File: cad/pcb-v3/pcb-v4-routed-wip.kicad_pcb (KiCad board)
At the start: 4 copper layers, 19.3 x 19.3 mm, 50 parts

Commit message: KiCad rewrites track geometry on format migration -- keep-out needs slack
The fill cleared blocker 18 and blocker 7 came back: three GND segments inside
the antenna keep-out, at coordinates that did not exist in the file I saved.

Diagnosis: not KiCad's fill and not the pour. Segment COUNT was identical in
and out (554), the keep-out polygons were byte-identical, but the geometry
moved. Opening the board migrated it from file format 20240108 to 20260206,
and the migration rewrote track geometry -- a tap path that skirted the
keep-out came back as a diagonal cutting the corner. Deepest copper intrusion
0.2635 mm.

So the previous commit's fix was necessary but not sufficient: honouring
'tracks not_allowed' stops US routing into the zone, and does nothing about
KiCad re-routing afterwards. The mask is now GROWN by halo + KEEPOUT_MARGIN
(0.30) to leave slack for whatever it simplifies into.

Two corrections to myself in this one:
  * my 'tracks not_allowed' fix carried a comment saying the mask was grown by
    the halo. It was not -- the comment described an intention, the code did
    a bare OR. Now there is a real _grow().
  * I first reached for 0.15 mm of margin and wrote that it 'covers it 10x
    over'. It does not: 0.15 < 0.2635, so it would have left the deepest
    intrusion in place. Sized from the measurement instead.

Costs 4 taps (24 -> 20). Paid deliberately -- copper in the antenna zone
cannot be seen, cannot be checked against a drawing, and ships as 'the radio
is mysteriously worse than it should be'.
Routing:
- net GND: track 11.8 -> 10.5 mm, vias 24 -> 20
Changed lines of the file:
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@@
 		)
 	)
-	(segment (start 5.7500 5.1500) (end 5.6500 5.1500) (width 0.127) (layer "F.Cu") (net 4))
-	(segment (start 5.6500 5.1500) (end 5.4000 4.9000) (width 0.127) (layer "F.Cu") (net 4))
-	(segment (start 5.4000 4.9000) (end 4.8000 4.9000) (width 0.127) (layer "F.Cu") (net 4))
-	(segment (start 4.8000 4.9000) (end 4.5000 4.6000) (width 0.127) (layer "F.Cu") (net 4))
 	(segment (start 2.8500 -8.6000) (end 2.6000 -8.8000) (width 0.127) (layer "F.Cu") (net 4))
 	(segment (start 2.6000 -8.8000) (end 1.5500 -8.8000) (width 0.127) (layer "F.Cu") (net 4))
 	(segment (start -3.4500 -8.6000) (end -3.6500 -8.6000) (width 0.127) (layer "F.Cu") (net 4))
 	(segment (start -3.6500 -8.6000) (end -3.7500 -8.5000) (width 0.127) (layer "F.Cu") (net 4))
-	(segment (start 6.1500 -8.3500) (end 6.4000 -8.6000) (width 0.127) (layer "F.Cu") (net 4))
+	(segment (start 5.6500 -8.3500) (end 6.0000 -8.7000) (width 0.127) (layer "F.Cu") (net 4))
 	(segment (start -8.3000 -3.3000) (end -8.6000 -3.3000) (width 0.127) (layer "B.Cu") (net 4))
 	(segment (start -8.6000 -3.3000) (end -8.9000 -3.6000) (width 0.127) (layer "B.Cu") (net 4))
@@
 	(segment (start -7.9000 1.7000) (end -8.2000 1.9500) (width 0.127) (layer "F.Cu") (net 4))
 	(segment (start -4.9500 -8.5500) (end -4.1000 -8.5500) (width 0.127) (layer "F.Cu") (net 4))
-	(via (at 4.5000 4.6000) (size 0.45) (drill 0.2) (layers "F.Cu" "B.Cu") (net 4))
-	(via (at 5.7500 6.9000) (size 0.45) (drill 0.2) (layers "F.Cu" "B.Cu") (net 4))
 	(via (at -3.9000 -8.4500) (size 0.45) (drill 0.2) (layers "F.Cu" "B.Cu") (net 4))
 	(via (at 7.1000 7.1500) (size 0.45) (drill 0.2) (layers "F.Cu" "B.Cu") (net 4))
 	(via (at -1.6500 -8.6000) (size 0.45) (drill 0.2) (layers "F.Cu" "B.Cu") (net 4))
 	(via (at 1.5500 -8.8000) (size 0.45) (drill 0.2) (layers "F.Cu" "B.Cu") (net 4))
-	(via (at 6.4000 -8.6000) (size 0.45) (drill 0.2) (layers "F.Cu" "B.Cu") (net 4))
+	(via (at 6.0000 -8.7000) (size 0.45) (drill 0.2) (layers "F.Cu" "B.Cu") (net 4))
 	(via (at -7.0000 2.7000) (size 0.45) (drill 0.2) (layers "F.Cu" "B.Cu") (net 4))
 	(via (at 1.0500 -8.3500) (size 0.45) (drill 0.2) (layers "F.Cu" "B.Cu") (net 4))
@@
 	(via (at 7.7500 7.1500) (size 0.45) (drill 0.2) (layers "F.Cu" "B.Cu") (net 4))
 	(via (at 4.7000 -6.4000) (size 0.45) (drill 0.2) (layers "F.Cu" "B.Cu") (net 4))
-	(via (at -5.7500 4.5500) (size 0.45) (drill 0.2) (layers "F.Cu" "B.Cu") (net 4))
 	(via (at -5.5500 -6.0000) (size 0.45) (drill 0.2) (layers "F.Cu" "B.Cu") (net 4))
 	(via (at -5.1500 3.4500) (size 0.45) (drill 0.2) (layers "F.Cu" "B.Cu") (net 4))
-	(via (at 3.5500 4.5500) (size 0.45) (drill 0.2) (layers "F.Cu" "B.Cu") (net 4))
 	(via (at 5.8500 -2.2500) (size 0.45) (drill 0.2) (layers "F.Cu" "B.Cu") (net 4))
 	(via (at 7.3000 -2.1000) (size 0.45) (drill 0.2) (layers "F.Cu" "B.Cu") (net 4))

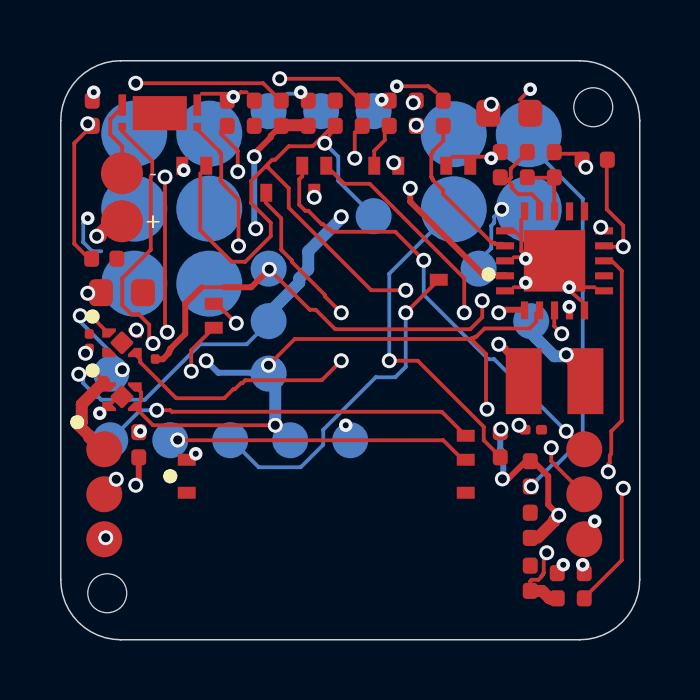
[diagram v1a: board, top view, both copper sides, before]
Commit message: gnd_taps: prune stub segments with a free end (and the custom-pad trap, again)
preflight check 20 caught two GND stubs on the filled board: (-8.30,-3.30),
which touched nothing at EITHER end, and (-2.10,-8.55), which ran from a via
to nowhere. Neither carried current, but a stub is an antenna, a yield
question, and a lie in the file about what is connected.

gnd_taps now prunes any tap segment whose end does not land on a GND pad, one
of its own vias, pre-existing GND copper, or another tap. Iterative, because
dropping a stub can orphan whatever fed it.

THE FIRST VERSION OF THIS PRUNE WAS WRONG and pruned 10 of 23 segments. Its
anchor test used max(w,h)/2, which for U3/U4 is the 0.1485 mm ANCHOR of a
custom pad, not its copper -- so every segment correctly landing on one looked
unanchored. That is the THIRD time this exact trap has bitten on this board
(stitch_open's masks, gnd_taps' own clearance masks, now this), and
pad_radius() -- the function written to avoid it -- was already defined 200
lines above. Fixed to use it: 4 stubs pruned, taps unchanged at 20.

Also corrected in passing: I claimed KiCad deleted 4 segments and 4 vias
during the fill. It did not. I compared the filled board against the PREVIOUS
revision instead of the file I actually saved; against the right baseline the
counts are identical at 550/84. The drop was my own 0.30 mm keep-out margin.

Antenna keep-out is clear and stayed clear through a fill -- the margin holds.
Blockers: 6 (8 open pads), 17 and 18 (the fill).
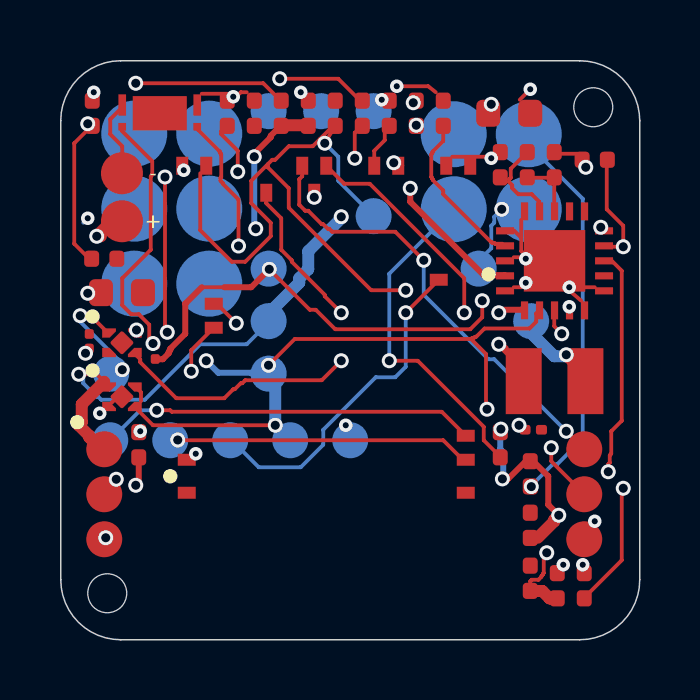
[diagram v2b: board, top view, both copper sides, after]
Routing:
- net GND: track 10.5 -> 8.83 mm
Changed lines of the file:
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@@
 	(segment (start -3.6500 -8.6000) (end -3.7500 -8.5000) (width 0.127) (layer "F.Cu") (net 4))
 	(segment (start 5.6500 -8.3500) (end 6.0000 -8.7000) (width 0.127) (layer "F.Cu") (net 4))
-	(segment (start -8.3000 -3.3000) (end -8.6000 -3.3000) (width 0.127) (layer "B.Cu") (net 4))
-	(segment (start -8.6000 -3.3000) (end -8.9000 -3.6000) (width 0.127) (layer "B.Cu") (net 4))
-	(segment (start -8.9000 -3.6000) (end -8.9000 -4.2500) (width 0.127) (layer "B.Cu") (net 4))
 	(segment (start -8.9000 -4.2500) (end -8.7500 -4.4000) (width 0.127) (layer "B.Cu") (net 4))
-	(segment (start -2.1000 -8.5500) (end -1.8000 -8.5500) (width 0.127) (layer "B.Cu") (net 4))
 	(segment (start 3.4000 -6.4500) (end 4.5500 -6.4500) (width 0.127) (layer "F.Cu") (net 4))
 	(segment (start 5.4500 -2.1000) (end 5.7000 -2.1000) (width 0.127) (layer "F.Cu") (net 4))

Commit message: gnd_taps: keep-out margin must not fence off pads OUTSIDE the keep-out
Down to 2 blockers, and the GND opens named their own cause: U1's GND pads sit
at y = 4.75 against an antenna keep-out starting at 4.95. Outside it -- but
buried under the 0.30 mm grown margin, so a tap could not start at the pad at
all. The margin exists to keep tracks OUT of the zone, not to fence off copper
beside it. Two GND pads went open purely because of my own fix.

masks() now applies the true keep-out ungrown and unconditional, and carves a
pad-sized escape disc out of the GROWN part only. Taps 20 -> 22; U1.1 and
U1.55 served again.

KNOWN RESIDUAL RISK, recorded rather than papered over: the escape discs
necessarily open holes in the margin, and four segments now sit 0.136-0.174 mm
from the keep-out where the margin wanted 0.30. KiCad's observed corner-cut
during format migration was 0.2635 mm, so these are inside the envelope of
what it could do. Zero segments are inside the keep-out as written; whether
that survives a KiCad round-trip is an empirical question and the fill/check
loop answers it directly. If blocker 7 returns at one of these four, the fix
is to drop the escape disc for that pad and let it go untapped -- a known-open
GND pad is a better failure than invisible antenna detuning.
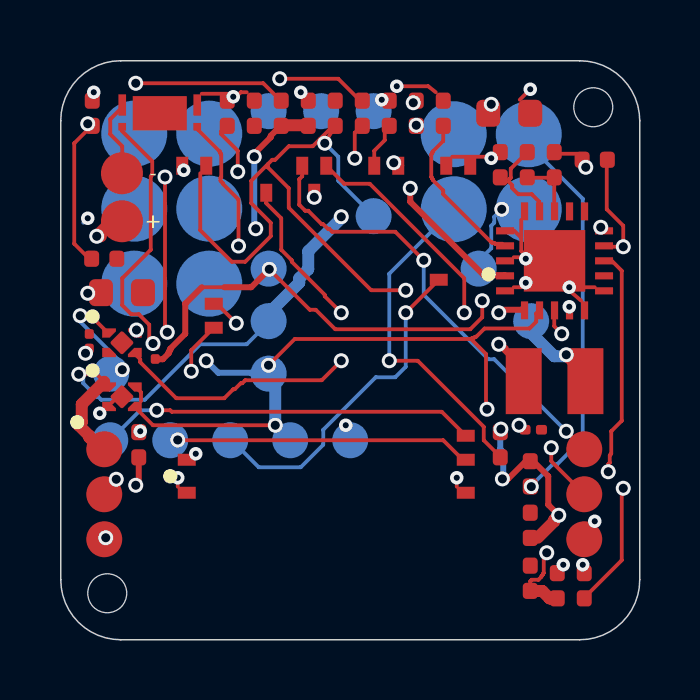
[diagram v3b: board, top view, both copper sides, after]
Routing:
- net GND: track 8.83 -> 9.43 mm, vias 20 -> 22
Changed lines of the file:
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@@
 	(segment (start 5.6500 -8.3500) (end 6.0000 -8.7000) (width 0.127) (layer "F.Cu") (net 4))
 	(segment (start -8.9000 -4.2500) (end -8.7500 -4.4000) (width 0.127) (layer "B.Cu") (net 4))
+	(segment (start -5.7500 4.5500) (end -5.7500 4.2500) (width 0.127) (layer "F.Cu") (net 4))
 	(segment (start 3.4000 -6.4500) (end 4.5500 -6.4500) (width 0.127) (layer "F.Cu") (net 4))
+	(segment (start 3.5500 4.5500) (end 3.5500 4.2500) (width 0.127) (layer "F.Cu") (net 4))
 	(segment (start 5.4500 -2.1000) (end 5.7000 -2.1000) (width 0.127) (layer "F.Cu") (net 4))
 	(segment (start 5.7000 -2.1000) (end 5.8500 -2.2500) (width 0.127) (layer "F.Cu") (net 4))
@@
 	(via (at 7.7500 7.1500) (size 0.45) (drill 0.2) (layers "F.Cu" "B.Cu") (net 4))
 	(via (at 4.7000 -6.4000) (size 0.45) (drill 0.2) (layers "F.Cu" "B.Cu") (net 4))
+	(via (at -5.7500 4.2500) (size 0.45) (drill 0.2) (layers "F.Cu" "B.Cu") (net 4))
 	(via (at -5.5500 -6.0000) (size 0.45) (drill 0.2) (layers "F.Cu" "B.Cu") (net 4))
 	(via (at -5.1500 3.4500) (size 0.45) (drill 0.2) (layers "F.Cu" "B.Cu") (net 4))
+	(via (at 3.5500 4.2500) (size 0.45) (drill 0.2) (layers "F.Cu" "B.Cu") (net 4))
 	(via (at 5.8500 -2.2500) (size 0.45) (drill 0.2) (layers "F.Cu" "B.Cu") (net 4))
 	(via (at 7.3000 -2.1000) (size 0.45) (drill 0.2) (layers "F.Cu" "B.Cu") (net 4))

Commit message: preflight check 22: no via may pierce a pogo contact -- BOTH boards fail it
THE BOARD IN THE CART FAILS THIS. pcb-v3-handoff.kicad_pcb, priced at $115.38
and waiting only on U1, has two vias drilled through J11's pogo contacts:
(2.95,-4.05) 0.580 mm into J11.3 and (2.40,-7.00) 0.331 mm into J11.1.
Pre-existing, and nothing to do with the PCM work.

A through-hole via over a pogo pad exits the underside in the middle of the
face the keyboard's sprung pin presses against. gnd_taps has refused to place
one since it was written -- but the rule lived in our scripts, not in the board
and not in the gate. So the router placed them, stitch_open placed another
(GND J4.5, 0.382 mm inside J4.5's own pad -- fixed today), and preflight had no
check at all. A rule enforced by the generators and not by the gate is a rule
you are relying on luck for.

stitch_open also gained the fab-floor via geometry; it had 0.60/0.30 hard-coded
while the floor now says 0.45/0.20 -- the same drift already fixed in gnd_taps
and handroute. Third instance.

Also fixed: stitch_open passed a relative board path to a subprocess it runs
with cwd=KRT, so check_connected looked in the wrong directory, found nothing,
and it reported 'nothing open' on a board with 8 open pads.

THREE ATTEMPTS AT THE UNDERLYING FIX ALL FAILED, recorded in
ROUTING-V4-STATUS.md: board-level keep-outs collapse the routing (8 -> 12
opens), deleting the vias costs 2 more opens because they are load-bearing, and
a targeted re-route of BL_RETURN + HARV_1 fails outright. Minimum legal ring is
1.45 mm and ten of them take too much board.

It is a design problem, not a tooling one: BL_RETURN and HARV_1 terminate on
B.Cu pogo pads, so reaching them from F.Cu needs a layer change, and there is
nowhere legal for the via. Probable answer is to keep both nets on B.Cu end to
end -- a topology change, not a router setting.
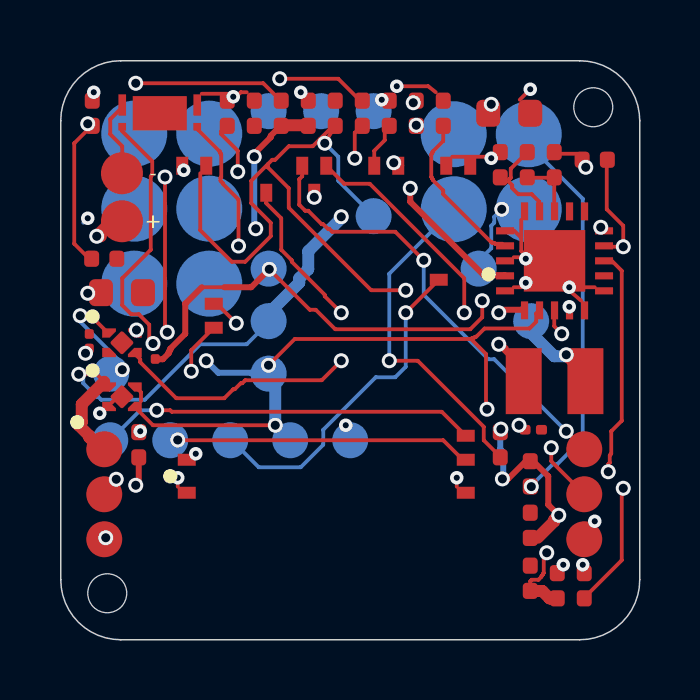
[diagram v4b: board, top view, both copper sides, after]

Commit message: v4 routing: pogo vias FIXED by routing those nets first -- check 22 passes
BL_RETURN and HARV_1..3 terminate on J11's B.Cu pads, so they need an
F.Cu->B.Cu via. Routed late, the only spot left is inside the pogo contact and
the router took it. Routed FIRST, with the 10 no-via rule areas (r = 1.45 mm =
pad 1.10 + via pad 0.25 + clearance 0.10) in place, ALL FOUR SUCCEED.

  22 no via pierces a pogo contact : PASS (82 vias vs 10 pogo pads, all clear)
  2  copper clearance              : PASS
  6b router DRC @ 0.10             : PASS
  7  antenna keep-out              : PASS

Three earlier attempts failed because they fought the symptom: blanket
keep-outs applied to a fully-routed board collapse it (8 -> 12 opens),
deleting the offending vias costs 2 opens because they are load-bearing, and a
targeted re-route of two nets into a full board fails outright. The rule was
always satisfiable. Ordering was the whole problem.

Stage 2 must EXCLUDE stage-1 nets BY NAME, not merely --keep-input-copper: left
in --nets '*', stage 2 rips and re-routes them, and PCM_VM lost its copper
exactly that way.

Recipe and the tooling traps written up in ROUTE-V4.md so this is reproducible
rather than folklore.
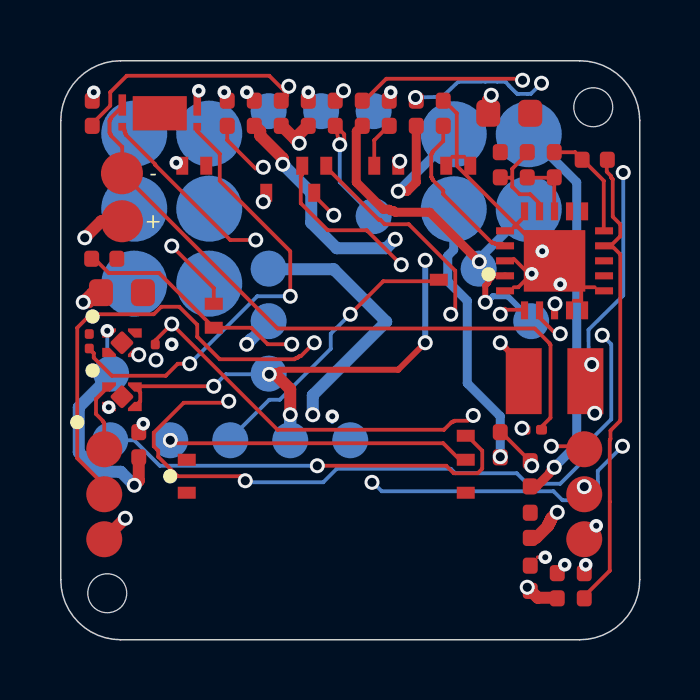
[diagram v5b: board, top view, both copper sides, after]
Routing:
- net BL_FLAG: track 16.5 -> 56.7 mm, vias 3 -> 6
- net VBAT_OK: track 42.4 -> 4.41 mm, vias 3 -> 1
- net CELL_NEG: track 2.66 -> 22.2 mm
- net VBAT: track 31.2 -> 43.4 mm, vias 5 -> 7
- net SENSOR_WAKEUP: track 12.8 -> 20.9 mm
- net SENSOR_SW_EN: track 14.8 -> 7.12 mm
- net PCM_VDD: track 31.0 -> 24.1 mm, vias 2 -> 4
- net VSTOR: track 50.0 -> 56.8 mm
- net RESET: track 11.3 -> 17.7 mm, vias 1 -> 2
- net VBAT_SENSE: track 23.9 -> 28.2 mm, vias 5 -> 2
- net PCM_VM: track 11.3 -> 15.2 mm
- net HARV_1: track 1.52 -> 5.29 mm
- net SENSOR_MCU_3V3: track 12.5 -> 10.1 mm, vias 4 -> 3
- net GND: track 9.43 -> 11.8 mm, vias 22 -> 18
- net HARV_3: track 11.2 -> 9.06 mm
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
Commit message: v4 status: 2 blockers, and the left strip is the real problem
Passing and holding through a KiCad round-trip: clearance, netlist<->board
(134 pins), dangling nets, router DRC, antenna keep-out, zone fill, dangling
ends, sourcing, and the new check 22 (no via pierces a pogo contact).

Remaining: 10 open pads and GND connectivity. FIVE of the ten are in the left
strip -- 2.72 mm wide, carrying U3, U4, C5, C12, R9 and C14, including two
TPS7A2033 in X2SON-4 whose pads are 0.34-0.40 mm apart when a 0.127 track needs
0.327 to pass. Six router configurations and three placement strategies have
all failed there. That is a placement problem; no router setting fixes a
2.72 mm channel with two fine-pitch QFNs in it.

Also recorded: stitch_open reports ROUTED for connections it does not make.
GND ROV1.2, U3.5 and J3.5 came back 'ROUTED' while check_connected -- which
models the fill and is preflight's gate -- still lists all three open, with a
byte-identical pad list before and after. ROV1 got '4 seg, 0 via': an F.Cu
track ending in free space, against a GND plane on In2.Cu that no F.Cu track
reaches without a via. own_copper() also still boxes custom pads at max(w,h)/2
-- fourth instance of that trap today. Its ROUTED count is not evidence.
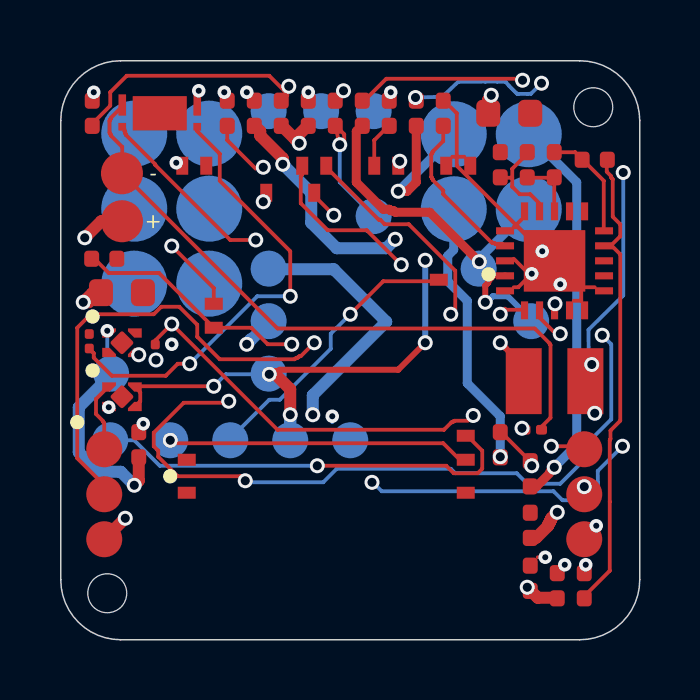
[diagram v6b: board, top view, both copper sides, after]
